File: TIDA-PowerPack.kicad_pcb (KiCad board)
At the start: 4 copper layers, 50 x 168 mm, 127 parts, among them Q3 IRFH5302TRPBF, Q4 IRFH5302TRPBF, SW1 SS-12M11G5, U1 TPS25750DRJKR, U10 XT30PW-F, U15 SB1045L_C2844167, U17 SMTSO3015CTJ, U18 SMTSO3015CTJ, U19 SMTSO3015CTJ, U2 CAT24C256WI-GT3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

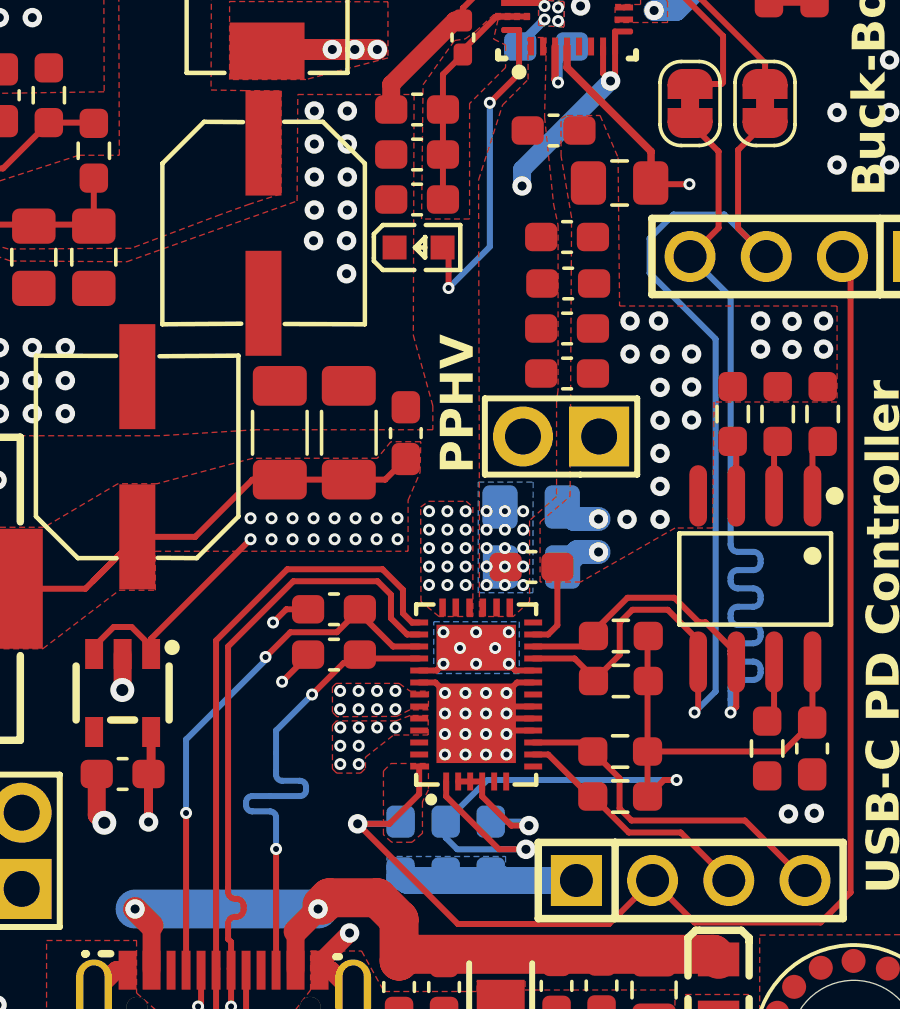
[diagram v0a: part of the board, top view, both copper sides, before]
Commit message: replace TPS25750D with TPS25751 chip
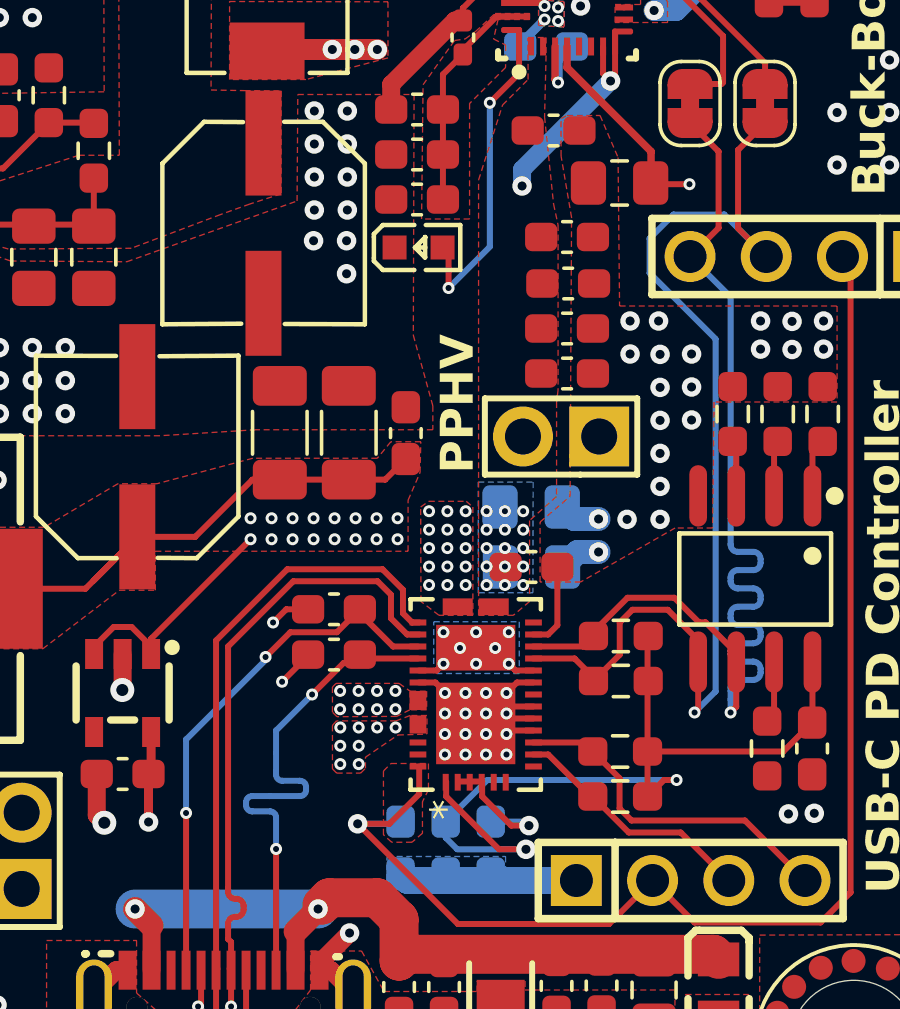
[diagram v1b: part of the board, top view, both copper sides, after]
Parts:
- removed U1: TPS25750DRJKR, easyeda2kicad:QFN-38_L6.0-W4.0-P0.40-TL-EP_RJK
- added U7: PTPS25751DREFR, TPS25751DREFR:WQFN38_REF_TEX, F.Cu at (150.4, 185.1)
